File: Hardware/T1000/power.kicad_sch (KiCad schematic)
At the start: 16 parts, among them J1 USB_C_Receptacle_USB2.0, J2 Conn_01x01_Male, J3 Conn_01x01_Male, J4 Conn_01x01_Male, J5 Conn_01x01_Male, U4 LTC4419, U5 LT6703HVCS5-3

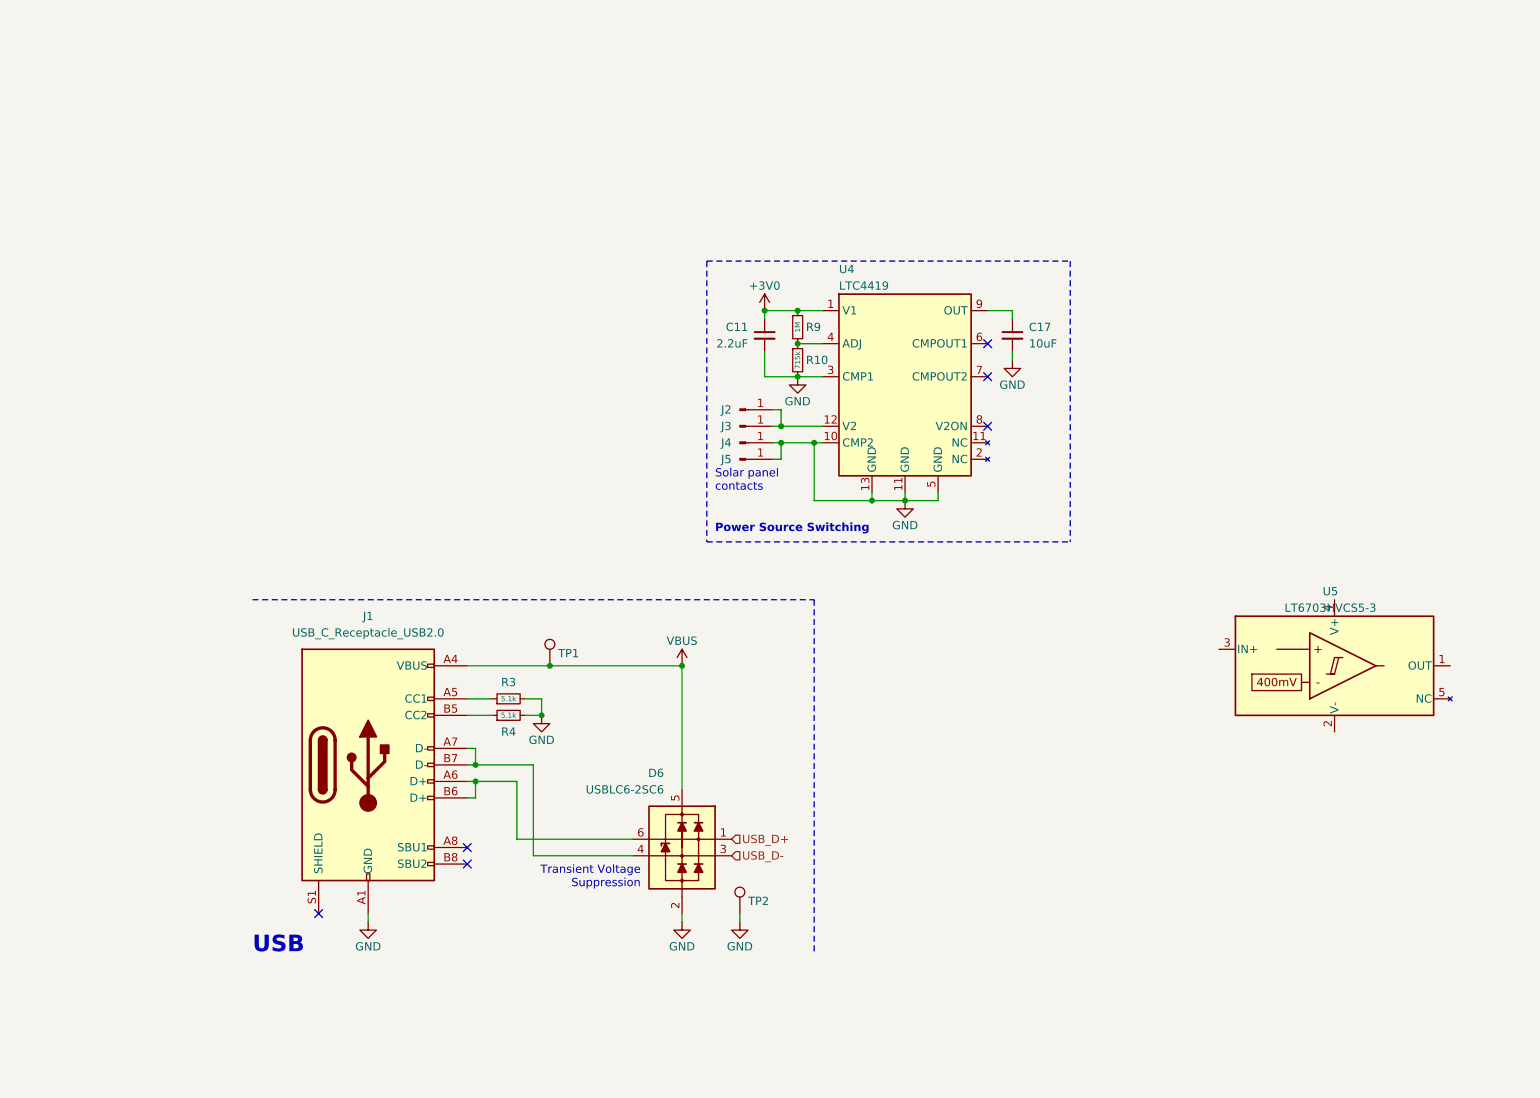
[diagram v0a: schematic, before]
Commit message: added SD card
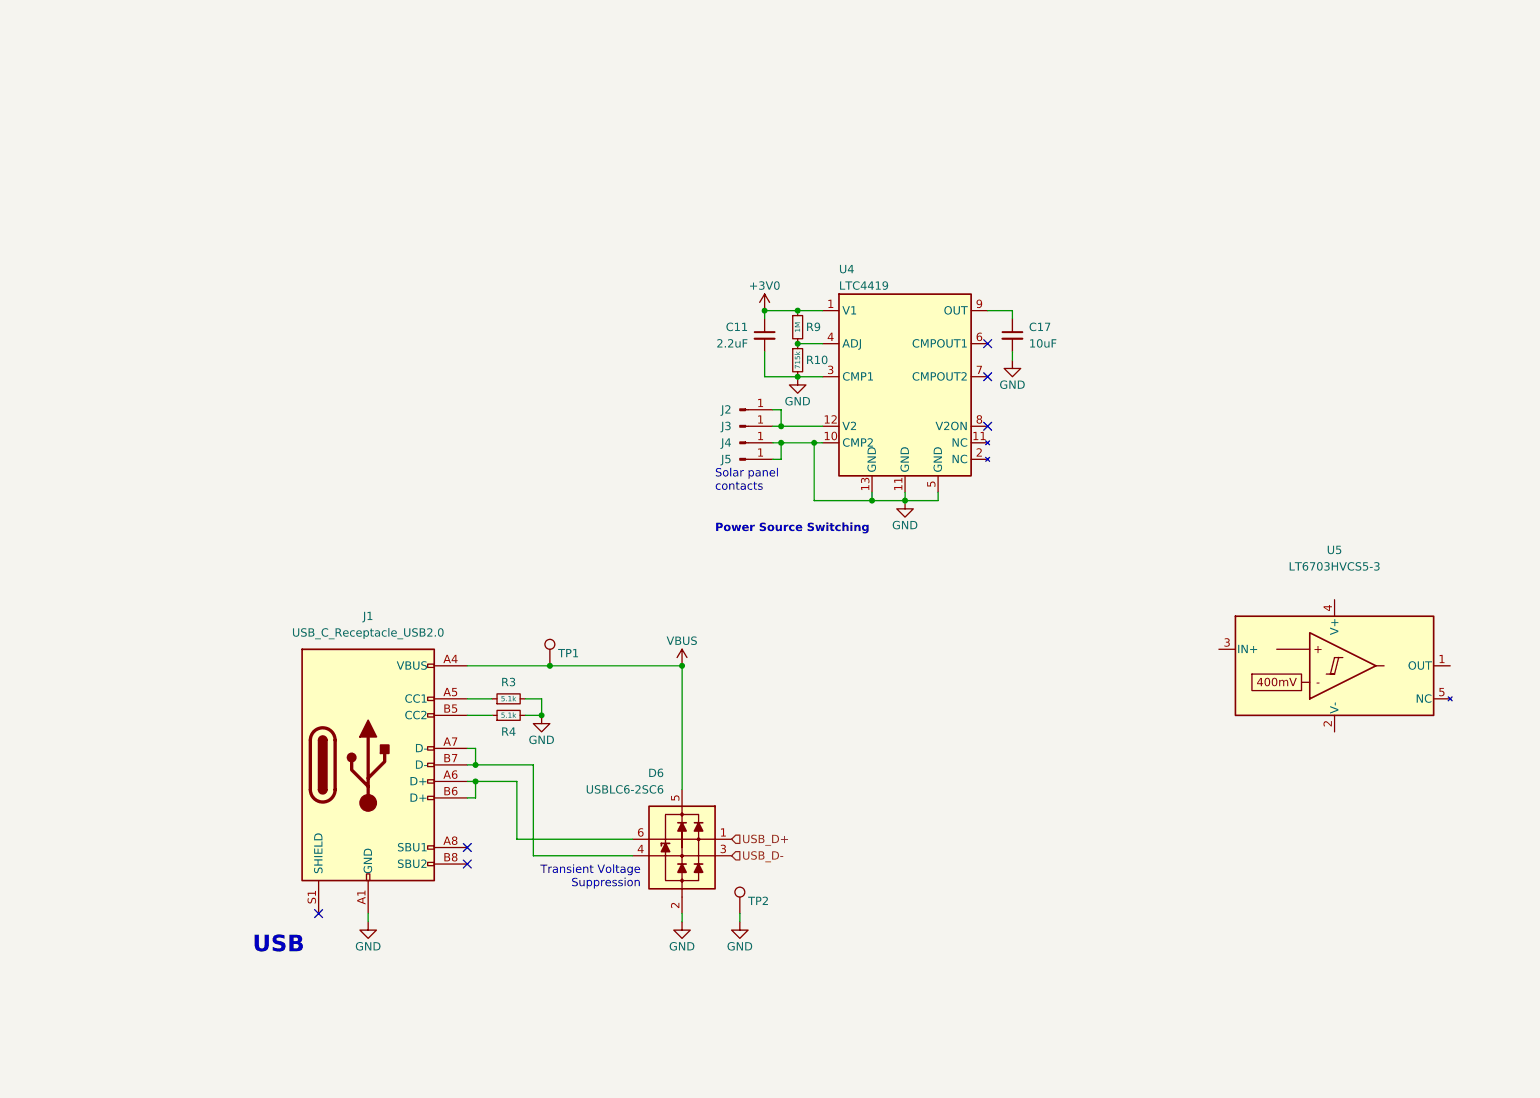
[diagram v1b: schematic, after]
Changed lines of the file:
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@@
     (stroke (width 0) (type default))
-  )
-  (polyline (pts (xy 57.15 107.95) (xy 143.51 107.95))
-    (stroke (width 0) (type dash))
   )
   (wire (pts (xy 91.44 130.81) (xy 91.44 133.35))
@@
     (stroke (width 0) (type default))
   )
-  (polyline (pts (xy 127 99.06) (xy 182.88 99.06))
-    (stroke (width 0) (type dash))
-  )
   (wire (pts (xy 99.06 125.73) (xy 101.6 125.73))
     (stroke (width 0) (type default))
@@
     (stroke (width 0) (type default))
   )
-  (polyline (pts (xy 127 55.88) (xy 127 99.06))
-    (stroke (width 0) (type dash))
-  )
   (wire (pts (xy 137.16 78.74) (xy 138.43 78.74))
     (stroke (width 0) (type default))
@@
     (stroke (width 0) (type default))
   )
-  (polyline (pts (xy 182.88 55.88) (xy 182.88 99.06))
-    (stroke (width 0) (type dash))
-  )
   (wire (pts (xy 140.97 68.58) (xy 144.78 68.58))
     (stroke (width 0) (type default))
@@
     (stroke (width 0) (type default))
   )
-  (polyline (pts (xy 127 55.88) (xy 182.88 55.88))
-    (stroke (width 0) (type dash))
-  )
   (wire (pts (xy 143.51 83.82) (xy 144.78 83.82))
     (stroke (width 0) (type default))
@@
   (wire (pts (xy 91.44 135.89) (xy 97.79 135.89))
     (stroke (width 0) (type default))
-  )
-  (polyline (pts (xy 143.51 107.95) (xy 143.51 162.56))
-    (stroke (width 0) (type dash))
   )
   (wire (pts (xy 157.48 91.44) (xy 157.48 92.71))
@@
   )
   (symbol (lib_id "PCM_Analog_Comparator_AKL:LT6703HVCS5-3") (at 223.52 118.11 0) (unit 1)
-    (in_bom yes) (on_board yes) (dnp no) (fields_autoplaced)
-    (property "Reference" "U5" (at 222.885 106.68 0)
+    (in_bom yes) (on_board yes) (dnp no)
+    (property "Reference" "U5" (at 223.52 100.33 0)
       (effects (font (size 1.27 1.27)))
     )
-    (property "Value" "LT6703HVCS5-3" (at 222.885 109.22 0)
+    (property "Value" "LT6703HVCS5-3" (at 223.52 102.87 0)
       (effects (font (size 1.27 1.27)))
     )

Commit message: buck-boost initial implementation
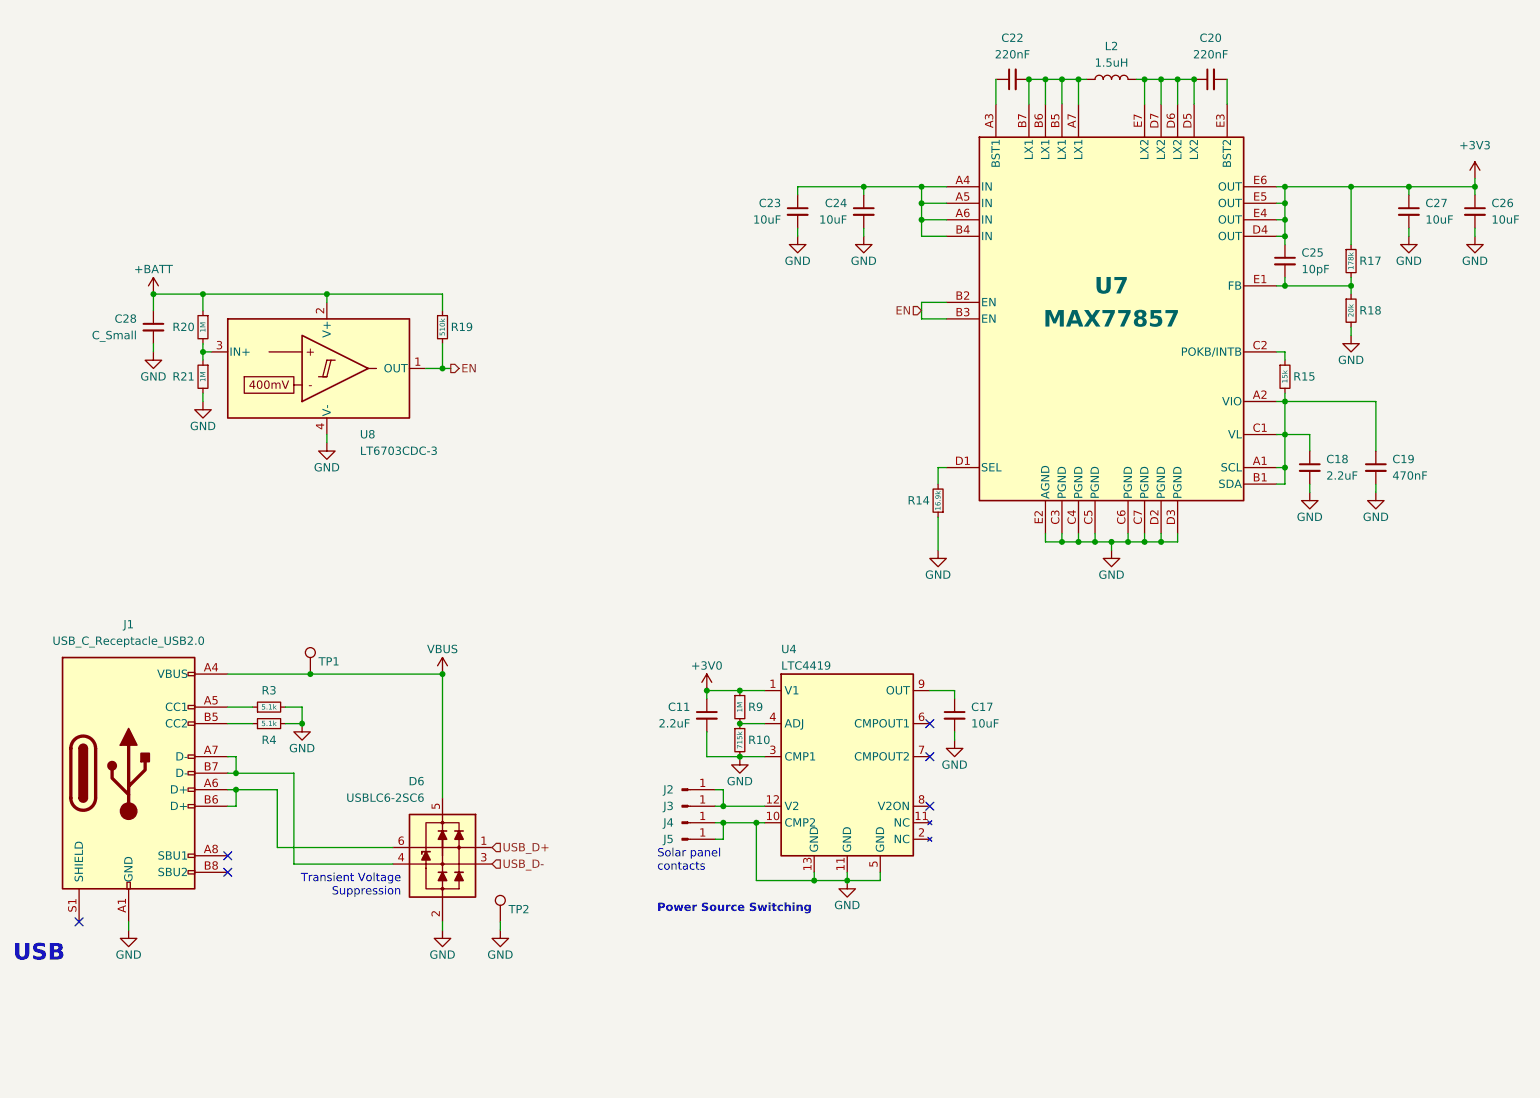
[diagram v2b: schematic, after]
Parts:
- removed U5: LT6703HVCS5-3, Package_TO_SOT_SMD_AKL:SOT-23-5, symbol PCM_Analog_Comparator_AKL:LT6703HVCS5-3
- added C18: 2.2uF, symbol Device:C_Small
- added C19: 470nF, symbol Device:C_Small
- added C20, C22: 220nF, symbol Device:C_Small
- added C23, C24, C26, C27: 10uF, symbol Device:C_Small
- added C25: 10pF, symbol Device:C_Small
- added C28: C_Small, symbol Device:C_Small
- added L2: 1.5uH, symbol Device:L
- added R14: 16.9k, symbol Device:R_Small
- added R15: 15k, symbol Device:R_Small
- added R17: 178k, symbol Device:R_Small
- added R18: 20k, symbol Device:R_Small
- added R19: 510k, symbol Device:R_Small
- added R20, R21: 1M, symbol Device:R_Small
- added U7: MAX77857, MAX77857:MAX77857-35WLP, symbol Power_Management:MAX77857BEWB+
- added U8: LT6703CDC-3, Package_DFN_QFN_AKL:DFN-3-1EP-2x2mm_P0.5mm_EP1x1.35mm, symbol PCM_Analog_Comparator_AKL:LT6703CDC-3
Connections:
- net GND: now also C18.2, C19.2, C23.2, C24.2, C26.2, C27.2, C28.2, R14.1, R18.2, R21.2, U7.C3 (PGND), U7.C4 (PGND), U7.C5 (PGND), U7.C6 (PGND), U7.C7 (PGND), U7.D2 (PGND), U7.D3 (PGND), U7.E2 (AGND), U8.4 (V-)
- new net: R15.1, U7.C2 (POKB/INTB)
- new net: C18.1, C19.1, R15.2, U7.A1 (SCL), U7.A2 (VIO), U7.B1 (SDA), U7.C1 (VL)
- new net: C22.1, U7.A3 (BST1)
- new net: C22.2, L2.1, U7.A7 (LX1), U7.B5 (LX1), U7.B6 (LX1), U7.B7 (LX1)
- new net: C25.2, R17.2, R18.1, U7.E1 (FB)
- new net: R20.2, R21.1, U8.3 (IN+)
- new net: C23.1, C24.1, U7.A4 (IN), U7.A5 (IN), U7.A6 (IN), U7.B4 (IN)
- new net: R14.2, U7.D1 (SEL)
- new net: C20.1, L2.2, U7.D5 (LX2), U7.D6 (LX2), U7.D7 (LX2), U7.E7 (LX2)
- new net: C20.2, U7.E3 (BST2)
- new net +3V3: C25.1, C26.1, C27.1, R17.1, U7.D4 (OUT), U7.E4 (OUT), U7.E5 (OUT), U7.E6 (OUT)
- new net +BATT: C28.1, R19.1, R20.1, U8.2 (V+)
- new net EN: R19.2, U7.B2 (EN), U7.B3 (EN), U8.1 (OUT)
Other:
- moved on the sheet: C11, C17, D6, J1, J2, J3, J4, J5, R10, R3, R4, R9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

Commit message: schematic updates
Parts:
- removed J2, J3, J4, J5: Conn_01x01_Male, Connector:P19-1121, symbol Connector:Conn_01x01_Male
- removed R15: 15k, symbol Device:R_Small
- added C29: C_Small, symbol Device:C_Small
- added L2: L, symbol Device:L
- added L3: L_Small, symbol Device:L_Small
- added R18: 100m, symbol Device:R_Small
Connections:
- net +3V0 is gone; now on net +BATT: C11.1, R9.1, U4.1 (V1)
- net +3V3: now also L2.1, L3.1
- net GND: now also C29.2
- net VBUS: now also U4.12 (V2)
- net SRC: now reaches C17.1, U4.9 (OUT)
- net SRC: now also C23.1, C24.1, U7.A4 (IN), U7.A5 (IN), U7.A6 (IN), U7.B4 (IN)
- net EN: no longer names the net of R19.2, U7.B2 (EN), U7.B3 (EN), U8.1 (OUT)
- new net: C29.1, L2.2, R18.2
- new net: L3.2, R18.1
- no-connect marks 6 -> 7
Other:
- note added: "Low Voltage Cutoff"
- note removed: "Solar panel contacts"
- company: (none) -> BPP
- title: (none) -> Terminator Power System
- moved on the sheet: C11, C17, C18, C19, C20, C22, C23, C24, C25, C26, C27, C28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
